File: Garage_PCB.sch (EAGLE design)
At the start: 20 parts, among them Q1 MOSFET-NCHANNELFQP30N06L-ALT

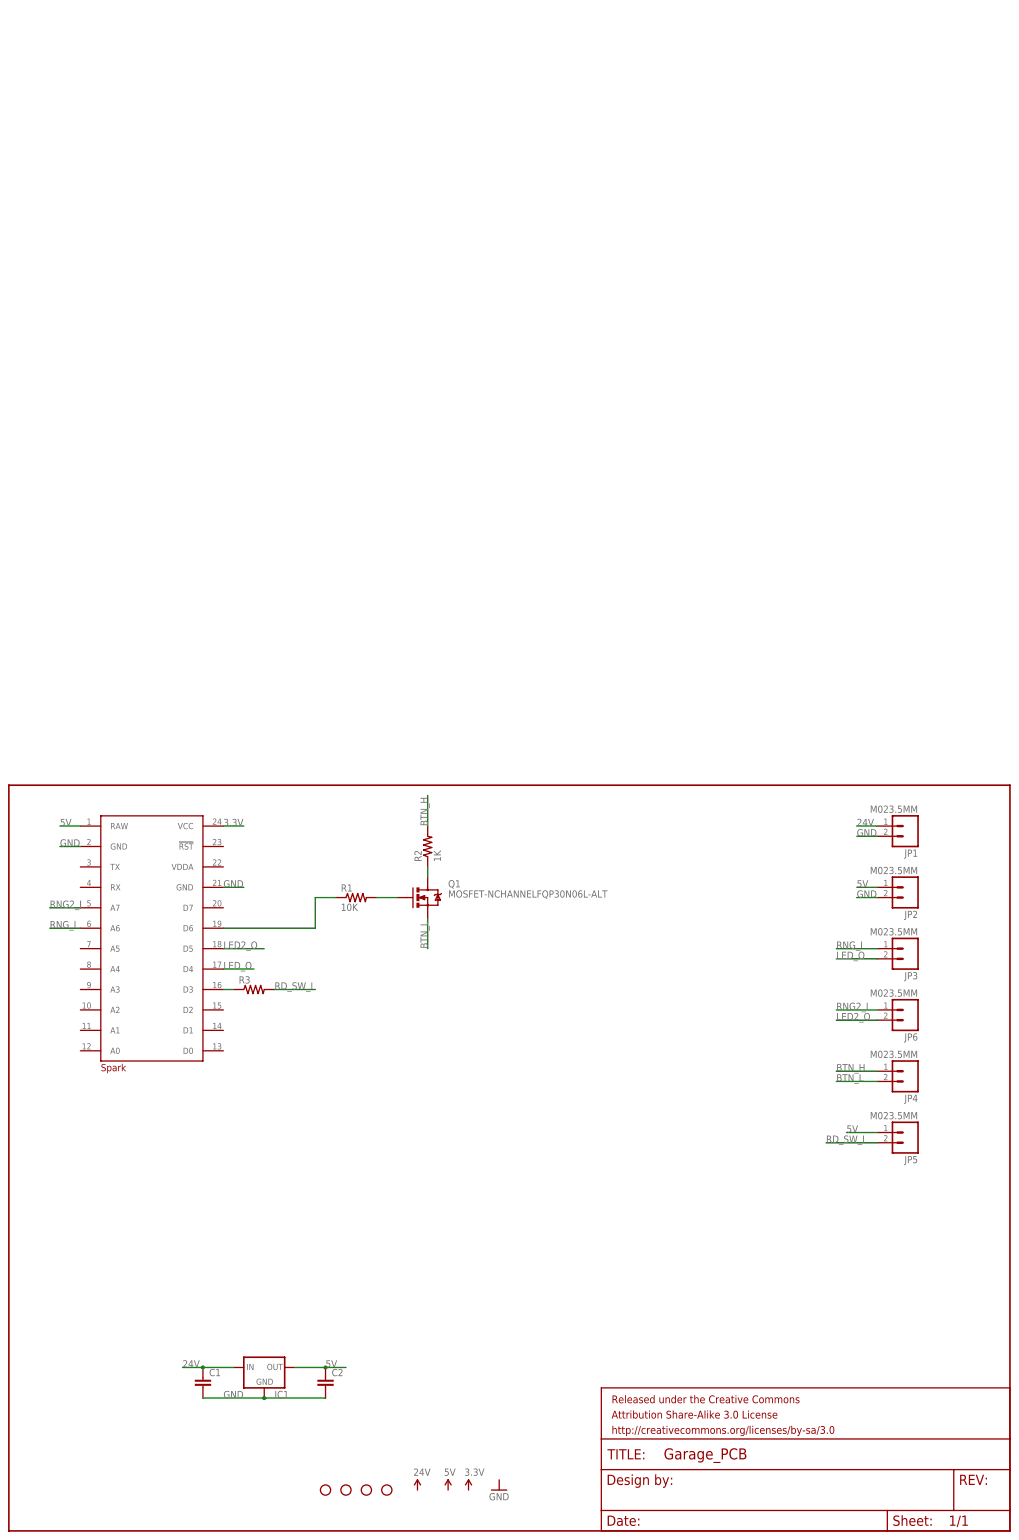
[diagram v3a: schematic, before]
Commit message: Moved the Mosfet to top layer
Moved the Mosfet to the top layer and made the necessary changes to the
board to connect it.  Also moved one of the Range finder pins to be
closer to the other.  Added a thermal pad to the Mosfet and added some
thermal vias.
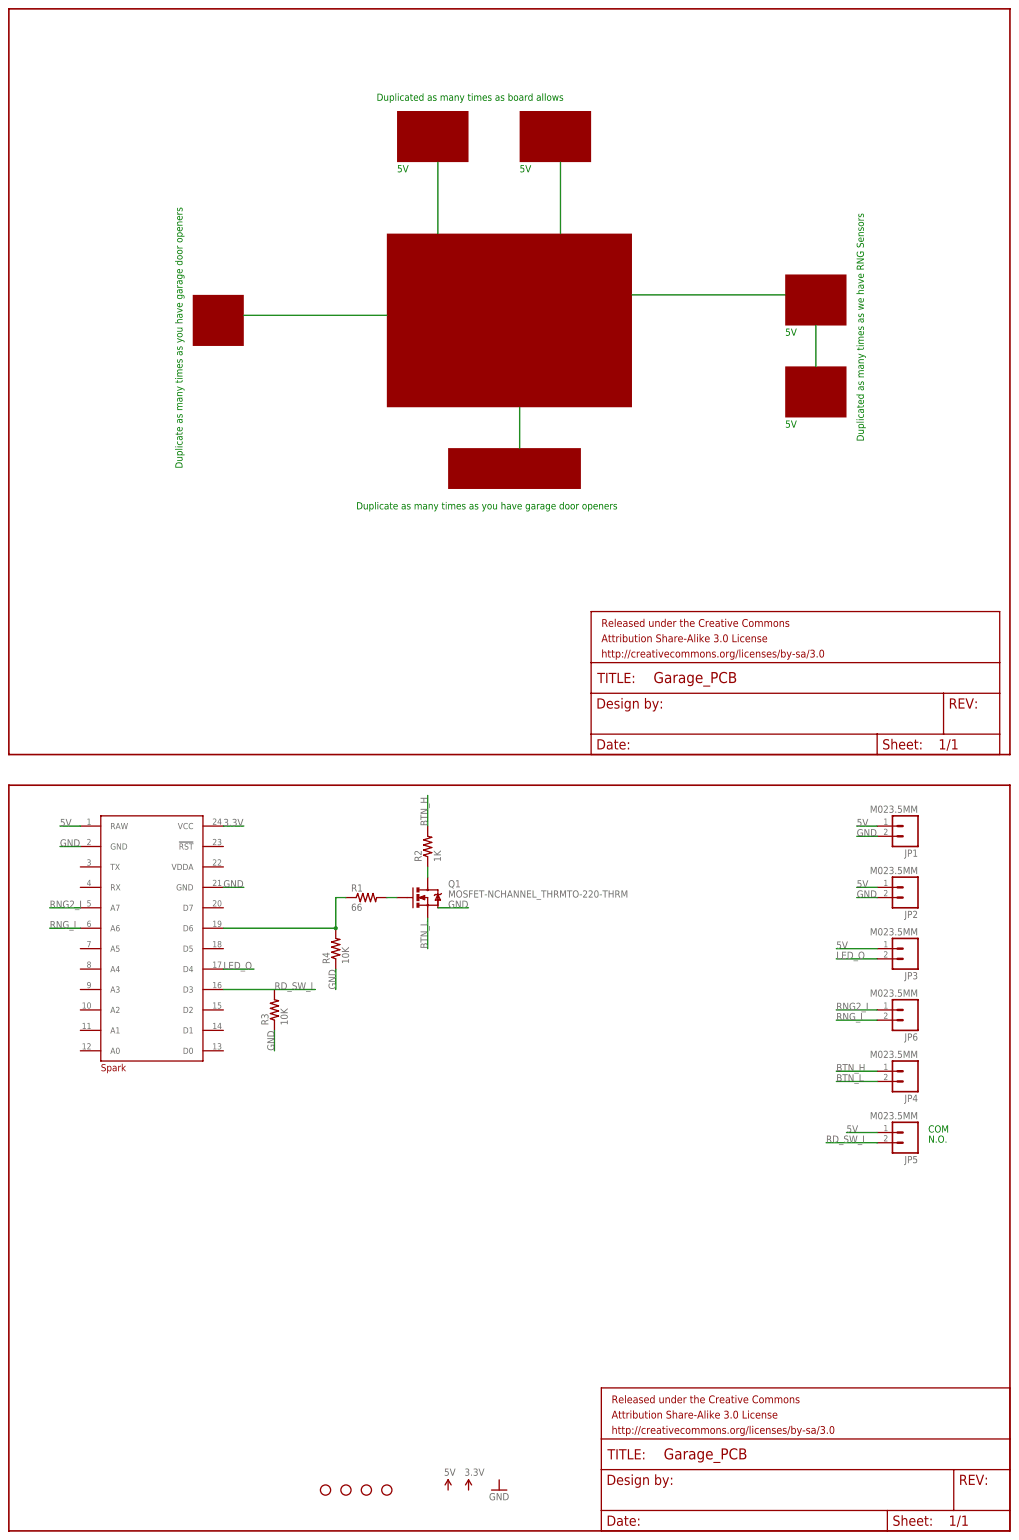
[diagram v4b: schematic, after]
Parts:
- removed C1, C2: (no value), SparkFun-Capacitors:CAP0603-CAP
- removed IC1: (no value), SparkFun-PowerIC:V_REG_78XX-TO-220
- added FRAME2: FRAME-LETTER, SparkFun-Aesthetics:FRAME-LETTER
- added R4: 10K, SparkFun-Resistors:RESISTOR0603
- Q1: value MOSFET-NCHANNELFQP30N06L-ALT -> MOSFET-NCHANNEL_THRMTO-220-THRM; device SparkFun-DiscreteSemi:MOSFET-NCHANNELFQP30N06L-ALT -> SparkFun-DiscreteSemi:MOSFET-NCHANNEL_THRMTO-220-THRM
- R1: value 10K -> 66
- R3: value (none) -> 10K
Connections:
- removed net 24V: C1.1, IC1.IN, JP1.1
- removed net LED2_O: JP6.2, SPARK.D5
- removed net N$1: R3.1, SPARK.D3
- net 5V: now also JP1.1, JP3.1; no longer C2.1, IC1.OUT
- net GND: now also Q1.THRM, R3.1, R4.1; no longer C1.2, C2.2, IC1.GND
- net N$15: now also R4.2
- net RD_SW_I: now also SPARK.D3
- net RNG_I: now also JP6.2; no longer JP3.1
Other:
- note added: "5V"
- note added: "COM"
- note added: "Duplicate as many times as you have garage door openers"
- note added: "Duplicated as many times as board allows"
- note added: "Duplicated as many times as we have RNG Sensors"
- note added: "FET"
- note added: "LED"
- note added: "N.O."
- note added: "REED SW"
- note added: "RNG SENS"
- note added: "Spark Core"
- moved on the sheet: R1, R3

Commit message: Added a pulldown to the BTN_L side
After some breadboard testing I found that the low side of the garage
door button needs to be pulled down to ground in order to de-energize
the line so that a new contact successfully gets registered.  Added this
pulldown and ordered this revision of the board.
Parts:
- added R5: 10K, SparkFun-Resistors:RESISTOR0603
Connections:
- net BTN_L: now also R5.2
- net GND: now also R5.1
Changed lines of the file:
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@@
 <part name="FRAME2" library="SparkFun-Aesthetics" deviceset="FRAME-LETTER" device=""/>
 <part name="JP1" library="SparkFun-Connectors" deviceset="M02" device="3.5MM"/>
+<part name="R5" library="SparkFun-Resistors" deviceset="RESISTOR" device="0603" value="10K"/>
 </parts>
 <sheets>
@@
 <instance part="FRAME2" gate="G$2" x="144.78" y="193.04"/>
 <instance part="JP1" gate="G$1" x="223.52" y="175.26" rot="R180"/>
+<instance part="R5" gate="G$1" x="109.22" y="147.32" rot="R180"/>
 </instances>
 <busses>
@@
 <wire x1="106.68" y1="154.94" x2="114.3" y2="154.94" width="0.2032" layer="91"/>
 <label x="109.22" y="154.94" size="1.778" layer="95"/>
+<pinref part="R5" gate="G$1" pin="1"/>
+<wire x1="114.3" y1="147.32" x2="114.3" y2="154.94" width="0.2032" layer="91"/>
+<wire x1="114.3" y1="154.94" x2="116.84" y2="154.94" width="0.2032" layer="91"/>
 </segment>
 </net>
@@
 <segment>
 <pinref part="Q1" gate="G$1" pin="S"/>
-<wire x1="104.14" y1="152.4" x2="104.14" y2="144.78" width="0.2032" layer="91"/>
+<wire x1="104.14" y1="152.4" x2="104.14" y2="147.32" width="0.2032" layer="91"/>
 <label x="104.14" y="144.78" size="1.778" layer="95" rot="R90"/>
-</segment>
-</net>
+<pinref part="R5" gate="G$1" pin="2"/>
+<wire x1="104.14" y1="147.32" x2="104.14" y2="144.78" width="0.2032" layer="91"/>
+<junction x="104.14" y="147.32"/>
+</segment>
+</net>

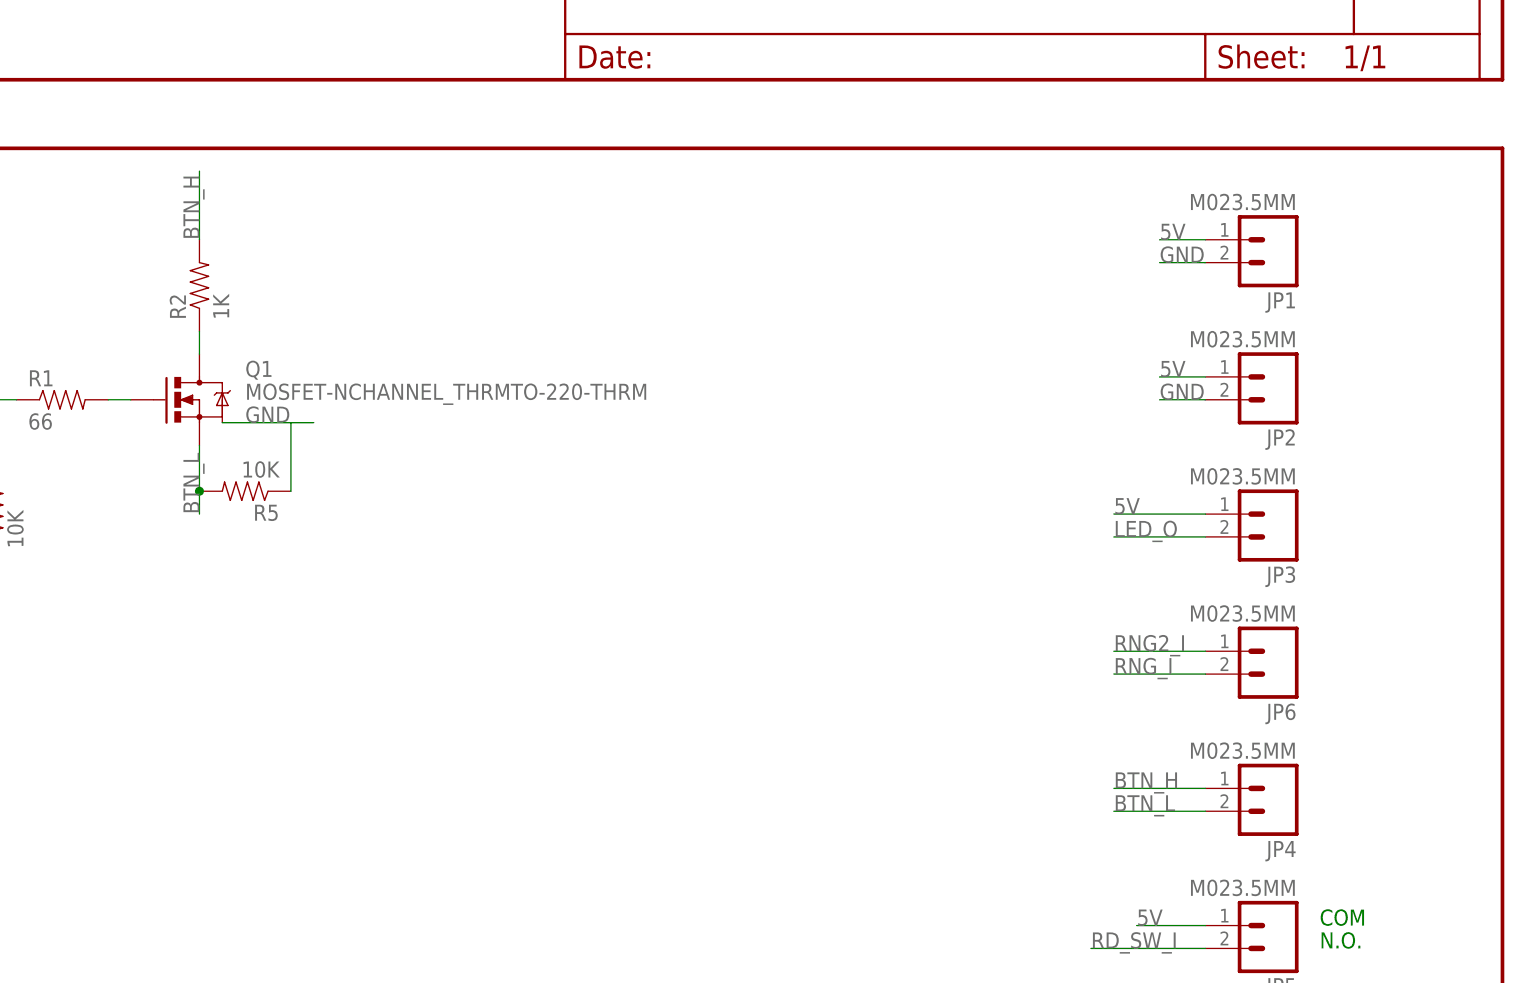
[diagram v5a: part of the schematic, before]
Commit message: Removed MOSFET inline resistors
The garage door button needs to have a direct connection from power
(btn_h) to ground (btn_l) in order to open or close the garage door.
The high side resistor kept this from happening.  I am not sure what I
was thinking with the low side 'pull down'.  This was just a weird
resistor connecting a groundplane on the opener to a ground plane on my
board.

I also renamed a few of the connection labels on the backside to be
correct.  The btn_p and btn_n were backwards and this was causing the
opener to not work.  The range finders also need to have different
labels so that the user knows which one is connected for configuring the
app/Spark Core.
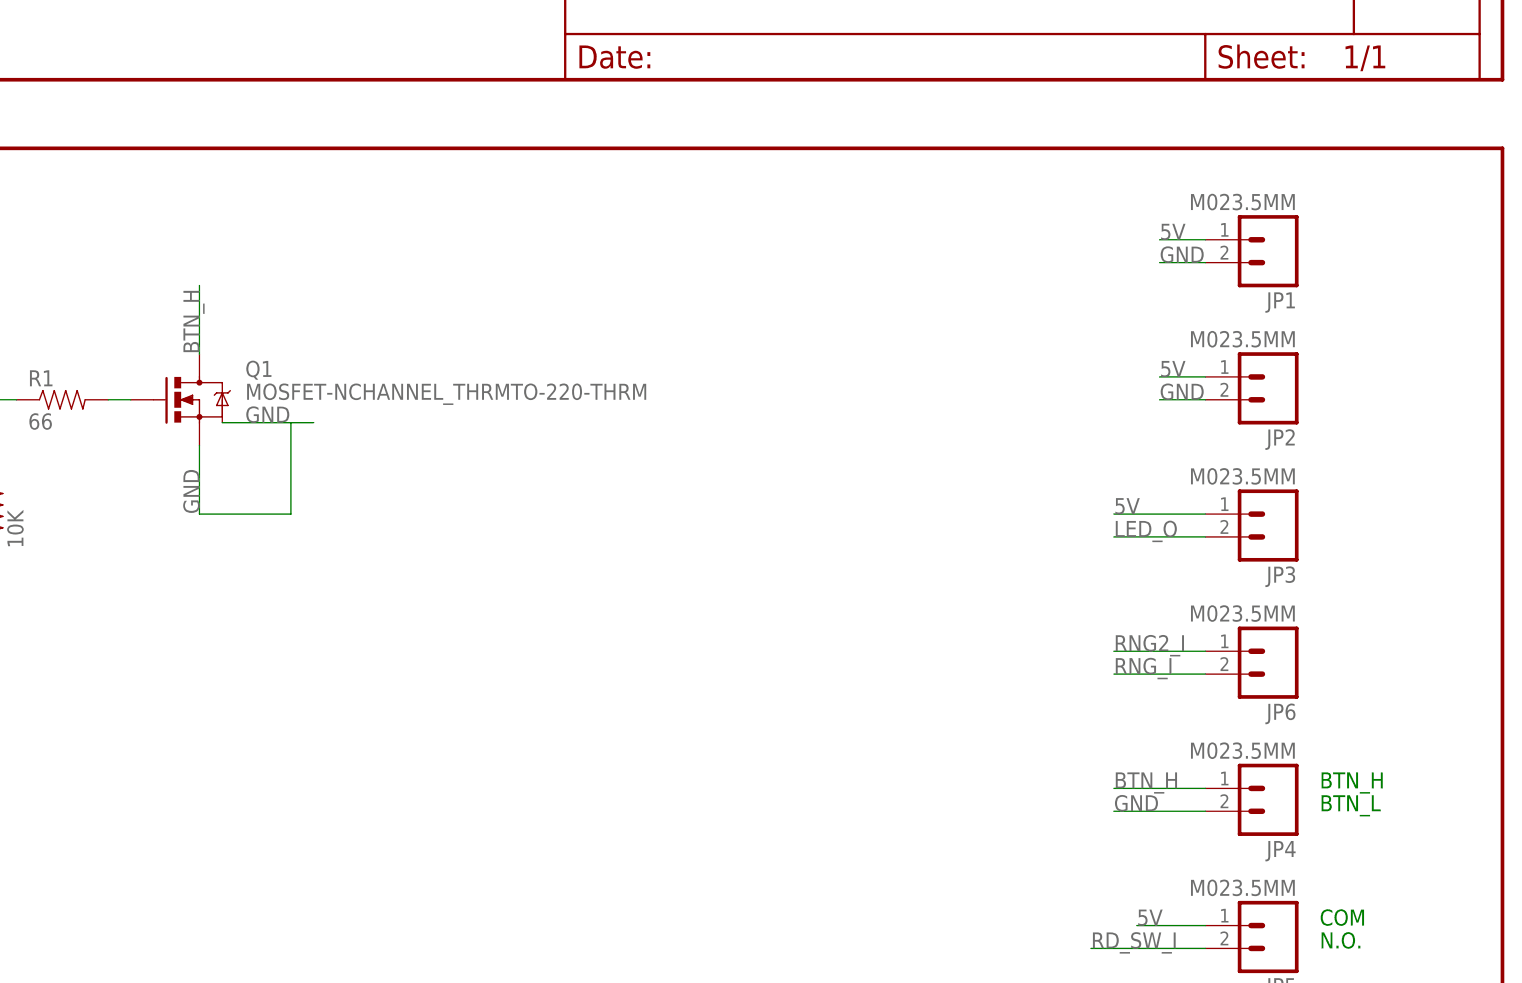
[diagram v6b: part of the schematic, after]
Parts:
- removed R2: 1K, SparkFun-Resistors:RESISTOR0603
- removed R5: 10K, SparkFun-Resistors:RESISTOR0603
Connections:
- removed net BTN_L: JP4.2, Q1.S, R5.2
- removed net N$17: Q1.D, R2.1
- net BTN_H: now also Q1.D; no longer R2.2
- net GND: now also JP4.2, Q1.S; no longer R5.1
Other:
- note added: "BTN_H"
- note added: "BTN_L"
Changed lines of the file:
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@@
 <part name="Q1" library="SparkFun-DiscreteSemi" deviceset="MOSFET-NCHANNEL_THRM" device="TO-220-THRM" value="MOSFET-NCHANNEL_THRMTO-220-THRM"/>
 <part name="R1" library="SparkFun-Resistors" deviceset="RESISTOR" device="0603" value="66"/>
-<part name="R2" library="SparkFun-Resistors" deviceset="RESISTOR" device="0603" value="1K"/>
 <part name="JP5" library="SparkFun-Connectors" deviceset="M02" device="3.5MM"/>
 <part name="R3" library="SparkFun-Resistors" deviceset="RESISTOR" device="0603" value="10K"/>
@@
 <part name="FRAME2" library="SparkFun-Aesthetics" deviceset="FRAME-LETTER" device=""/>
 <part name="JP1" library="SparkFun-Connectors" deviceset="M02" device="3.5MM"/>
-<part name="R5" library="SparkFun-Resistors" deviceset="RESISTOR" device="0603" value="10K"/>
 </parts>
 <sheets>
@@
 <text x="193.04" y="297.18" size="1.778" layer="91">5V</text>
 <text x="193.04" y="274.32" size="1.778" layer="91">5V</text>
+<text x="228.6" y="111.76" size="1.778" layer="91">BTN_L</text>
+<text x="228.6" y="114.3" size="1.778" layer="91">BTN_H</text>
 </plain>
 <instances>
@@
 <instance part="Q1" gate="G$1" x="104.14" y="157.48"/>
 <instance part="R1" gate="G$1" x="88.9" y="157.48"/>
-<instance part="R2" gate="G$1" x="104.14" y="170.18" rot="R90"/>
 <instance part="JP5" gate="G$1" x="223.52" y="99.06" rot="R180"/>
 <instance part="R3" gate="G$1" x="66.04" y="129.54" rot="R90"/>
@@
 <instance part="FRAME2" gate="G$2" x="144.78" y="193.04"/>
 <instance part="JP1" gate="G$1" x="223.52" y="175.26" rot="R180"/>
-<instance part="R5" gate="G$1" x="109.22" y="147.32" rot="R180"/>
 </instances>
 <busses>
@@
 <wire x1="106.68" y1="154.94" x2="114.3" y2="154.94" width="0.2032" layer="91"/>
 <label x="109.22" y="154.94" size="1.778" layer="95"/>
-<pinref part="R5" gate="G$1" pin="1"/>
-<wire x1="114.3" y1="147.32" x2="114.3" y2="154.94" width="0.2032" layer="91"/>
+<wire x1="114.3" y1="144.78" x2="114.3" y2="154.94" width="0.2032" layer="91"/>
 <wire x1="114.3" y1="154.94" x2="116.84" y2="154.94" width="0.2032" layer="91"/>
+<pinref part="Q1" gate="G$1" pin="S"/>
+<wire x1="104.14" y1="152.4" x2="104.14" y2="144.78" width="0.2032" layer="91"/>
+<label x="104.14" y="144.78" size="1.778" layer="95" rot="R90"/>
+<wire x1="114.3" y1="144.78" x2="104.14" y2="144.78" width="0.2032" layer="91"/>
+</segment>
+<segment>
+<pinref part="JP4" gate="G$1" pin="2"/>
+<wire x1="215.9" y1="111.76" x2="205.74" y2="111.76" width="0.2032" layer="91"/>
+<label x="205.74" y="111.76" size="1.778" layer="95"/>
 </segment>
 </net>
@@
 <wire x1="215.9" y1="144.78" x2="205.74" y2="144.78" width="0.2032" layer="91"/>
 <label x="205.74" y="144.78" size="1.778" layer="95"/>
-</segment>
-</net>
-<net name="N$17" class="0">
-<segment>
-<pinref part="Q1" gate="G$1" pin="D"/>
-<wire x1="104.14" y1="162.56" x2="104.14" y2="165.1" width="0.2032" layer="91"/>
-<pinref part="R2" gate="G$1" pin="1"/>
 </segment>
 </net>
@@
 </segment>
 <segment>
-<pinref part="R2" gate="G$1" pin="2"/>
-<wire x1="104.14" y1="175.26" x2="104.14" y2="182.88" width="0.2032" layer="91"/>
-<label x="104.14" y="175.26" size="1.778" layer="95" rot="R90"/>
-</segment>
-</net>
-<net name="BTN_L" class="0">
-<segment>
-<pinref part="JP4" gate="G$1" pin="2"/>
-<wire x1="215.9" y1="111.76" x2="205.74" y2="111.76" width="0.2032" layer="91"/>
-<label x="205.74" y="111.76" size="1.778" layer="95"/>
-</segment>
-<segment>
-<pinref part="Q1" gate="G$1" pin="S"/>
-<wire x1="104.14" y1="152.4" x2="104.14" y2="147.32" width="0.2032" layer="91"/>
-<label x="104.14" y="144.78" size="1.778" layer="95" rot="R90"/>
-<pinref part="R5" gate="G$1" pin="2"/>
-<wire x1="104.14" y1="147.32" x2="104.14" y2="144.78" width="0.2032" layer="91"/>
-<junction x="104.14" y="147.32"/>
-</segment>
-</net>
+<wire x1="104.14" y1="162.56" x2="104.14" y2="170.18" width="0.2032" layer="91"/>
+<label x="104.14" y="162.56" size="1.778" layer="95" rot="R90"/>
+<pinref part="Q1" gate="G$1" pin="D"/>
+</segment>
+</net>
